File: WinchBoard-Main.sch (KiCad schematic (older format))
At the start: 26 parts, among them J1 HDMI_A, P1 CONN_01X04, P2 CONN_01X04, P3 CONN_01X04, P4 CONN_01X02, P5 CONN_01X02, P6 CONN_01X02, P7 CONN_01X03

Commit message: Checkpoint - component placement
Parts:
- added TT10, TT12: GND, _Connector:Test_Point_SMD_0.040_Top, symbol TP_Top
- added TT13: GNDA, _Connector:Test_Point_SMD_0.040_Top, symbol TP_Top
- P1, P2, P3: footprint Connectors_Molex:Molex_KK-6410-04_04x2.54mm_Straight -> _Connector:Molex_KK-6410-04_04x2.54mm_Straight
- P4, P5: footprint Connectors_Molex:Molex_KK-6410-02_02x2.54mm_Straight -> _Connector:Molex_KK-6410-02_02x2.54mm_Straight
- P6: footprint Connectors_Molex:Molex_KK-6410-02_02x2.54mm_Straight -> _Connector:0.100_1x2_small
- renumbered TT10 to TT11, TT11 to TT14
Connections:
- net GNDA: now also TT13.1 (TP)
- net GNDD: now also TT10.1 (TP), TT12.1 (TP)
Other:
- moved on the sheet: TT11, TT14
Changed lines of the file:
@@
 F 0 "P5" H 5400 4650 50  0000 C CNN
 F 1 "CONN_01X02" V 5500 4500 50  0000 C CNN
-F 2 "Connectors_Molex:Molex_KK-6410-02_02x2.54mm_Straight" H 5400 4500 50  0001 C CNN
+F 2 "_Connector:Molex_KK-6410-02_02x2.54mm_Straight" H 5400 4500 50  0001 C CNN
 F 3 "" H 5400 4500 50  0000 C CNN
 	1    5400 4500
@@
 F 0 "P3" H 4650 2900 50  0000 C CNN
 F 1 "CONN_01X04" V 4750 2650 50  0000 C CNN
-F 2 "Connectors_Molex:Molex_KK-6410-04_04x2.54mm_Straight" H 4650 2650 50  0001 C CNN
+F 2 "_Connector:Molex_KK-6410-04_04x2.54mm_Straight" H 4650 2650 50  0001 C CNN
 F 3 "" H 4650 2650 50  0000 C CNN
 	1    4650 2650
@@
 F 0 "P2" H 3650 3400 50  0000 C CNN
 F 1 "CONN_01X04" V 3750 3150 50  0000 C CNN
-F 2 "Connectors_Molex:Molex_KK-6410-04_04x2.54mm_Straight" H 3650 3150 50  0001 C CNN
+F 2 "_Connector:Molex_KK-6410-04_04x2.54mm_Straight" H 3650 3150 50  0001 C CNN
 F 3 "" H 3650 3150 50  0000 C CNN
 	1    3650 3150
@@
 L +Vanalog #PWR04
 U 1 1 5B94F6C9
-P 6750 1300
-F 0 "#PWR04" H 6750 1150 50  0001 C CNN
-F 1 "+Vanalog" H 6750 1440 50  0000 C CNN
-F 2 "" H 6750 1300 50  0000 C CNN
-F 3 "" H 6750 1300 50  0000 C CNN
-	1    6750 1300
+P 6650 1300
+F 0 "#PWR04" H 6650 1150 50  0001 C CNN
+F 1 "+Vanalog" H 6650 1440 50  0000 C CNN
+F 2 "" H 6650 1300 50  0000 C CNN
+F 3 "" H 6650 1300 50  0000 C CNN
+	1    6650 1300
 	1    0    0    -1
 $EndComp
@@
 F 0 "P1" H 2750 3900 50  0000 C CNN
 F 1 "CONN_01X04" V 2850 3650 50  0000 C CNN
-F 2 "Connectors_Molex:Molex_KK-6410-04_04x2.54mm_Straight" H 2750 3650 50  0001 C CNN
+F 2 "_Connector:Molex_KK-6410-04_04x2.54mm_Straight" H 2750 3650 50  0001 C CNN
 F 3 "" H 2750 3650 50  0000 C CNN
 	1    2750 3650
@@
 F 0 "P4" H 5150 4300 50  0000 C CNN
 F 1 "CONN_01X02" V 5250 4150 50  0000 C CNN
-F 2 "Connectors_Molex:Molex_KK-6410-02_02x2.54mm_Straight" H 5150 4150 50  0001 C CNN
+F 2 "_Connector:Molex_KK-6410-02_02x2.54mm_Straight" H 5150 4150 50  0001 C CNN
 F 3 "" H 5150 4150 50  0000 C CNN
 	1    5150 4150
@@
 	6500 2000 6800 2000
 Wire Wire Line
-	6750 1300 6750 2000
-Connection ~ 6750 2000
+	6650 1300 6650 2000
+Connection ~ 6650 2000
 Wire Wire Line
 	6500 2100 6800 2100
 Wire Wire Line
-	6750 2100 6750 2250
+	6750 1950 6750 2250
 Connection ~ 6750 2100
 Wire Wire Line
-	6800 2200 6500 2200
+	6500 2200 6800 2200
 Wire Wire Line
 	4850 2800 6100 2800
@@
 Connection ~ 6200 4400
 $Comp
-L TP_Top TT11
+L TP_Top TT14
 U 1 1 5B952A2E
-P 6950 1450
-F 0 "TT11" H 7000 1480 35  0000 C CNN
-F 1 "+Vanalog" H 6960 1580 50  0000 C CNN
-F 2 "_Connector:Test_Point_SMD_0.040_Top" H 6950 1500 50  0001 C CNN
-F 3 "" H 6950 1500 50  0000 C CNN
-	1    6950 1450
+P 6850 1450
+F 0 "TT14" H 6900 1480 35  0000 C CNN
+F 1 "+Vanalog" H 6860 1580 50  0000 C CNN
+F 2 "_Connector:Test_Point_SMD_0.040_Top" H 6850 1500 50  0001 C CNN
+F 3 "" H 6850 1500 50  0000 C CNN
+	1    6850 1450
 	1    0    0    -1
 $EndComp
@@
 $EndComp
 Wire Wire Line
-	6750 1500 6950 1500
-Wire Wire Line
-	6950 1500 6950 1450
-Connection ~ 6750 1500
+	6650 1500 6850 1500
+Wire Wire Line
+	6850 1500 6850 1450
+Connection ~ 6650 1500
 Wire Wire Line
 	6100 1500 6300 1500
@@
 F 0 "P6" H 5600 5050 50  0000 C CNN
 F 1 "CONN_01X02" V 5700 4900 50  0000 C CNN
-F 2 "Connectors_Molex:Molex_KK-6410-02_02x2.54mm_Straight" H 5600 4900 50  0001 C CNN
+F 2 "_Connector:0.100_1x2_small" H 5600 4900 50  0001 C CNN
 F 3 "" H 5600 4900 50  0000 C CNN
 	1    5600 4900
@@
 Group D Twisted Pair
 $Comp
+L TP_Top TT11
+U 1 1 5B958039
+P 6550 1900
+F 0 "TT11" H 6600 1930 35  0000 C CNN
+F 1 "Aout" H 6560 2030 50  0000 C CNN
+F 2 "_Connector:Test_Point_SMD_0.040_Top" H 6550 1950 50  0001 C CNN
+F 3 "" H 6550 1950 50  0000 C CNN
+	1    6550 1900
+	1    0    0    -1
+$EndComp
+Wire Wire Line
+	6550 1900 6550 2200
+Connection ~ 6550 2200
+$Comp
 L TP_Top TT10
-U 1 1 5B958039
-P 6550 1950
-F 0 "TT10" H 6600 1980 35  0000 C CNN
-F 1 "Aout" H 6560 2080 50  0000 C CNN
-F 2 "_Connector:Test_Point_SMD_0.040_Top" H 6550 2000 50  0001 C CNN
-F 3 "" H 6550 2000 50  0000 C CNN
-	1    6550 1950
-	1    0    0    -1
-$EndComp
-Wire Wire Line
-	6550 1950 6550 2200
-Connection ~ 6550 2200
+U 1 1 5B952974
+P 6500 4900
+F 0 "TT10" H 6550 4930 35  0000 C CNN
+F 1 "GND" H 6510 5030 50  0000 C CNN
+F 2 "_Connector:Test_Point_SMD_0.040_Top" H 6500 4950 50  0001 C CNN
+F 3 "" H 6500 4950 50  0000 C CNN
+	1    6500 4900
+	1    0    0    -1
+$EndComp
+$Comp
+L TP_Top TT12
+U 1 1 5B9529E6
+P 6750 4900
+F 0 "TT12" H 6800 4930 35  0000 C CNN
+F 1 "GND" H 6760 5030 50  0000 C CNN
+F 2 "_Connector:Test_Point_SMD_0.040_Top" H 6750 4950 50  0001 C CNN
+F 3 "" H 6750 4950 50  0000 C CNN
+	1    6750 4900
+	1    0    0    -1
+$EndComp
+Wire Wire Line
+	6500 4900 6500 4950
+Connection ~ 6500 4950
+Wire Wire Line
+	6750 4900 6750 4950
+Connection ~ 6750 4950
+$Comp
+L TP_Top TT13
+U 1 1 5B952D09
+P 6800 1900
+F 0 "TT13" H 6850 1930 35  0000 C CNN
+F 1 "GNDA" H 6810 2030 50  0000 C CNN
+F 2 "_Connector:Test_Point_SMD_0.040_Top" H 6800 1950 50  0001 C CNN
+F 3 "" H 6800 1950 50  0000 C CNN
+	1    6800 1900
+	1    0    0    -1
+$EndComp
+Wire Wire Line
+	6750 1950 6800 1950
+Wire Wire Line
+	6800 1950 6800 1900
 $EndSCHEMATC

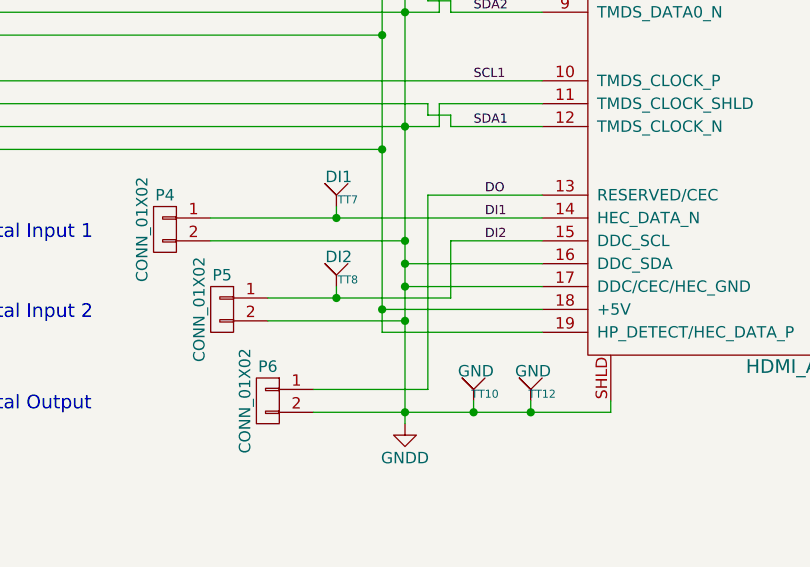
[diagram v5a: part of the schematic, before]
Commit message: Version 001 - 1.4” x 1/6” locking connectors
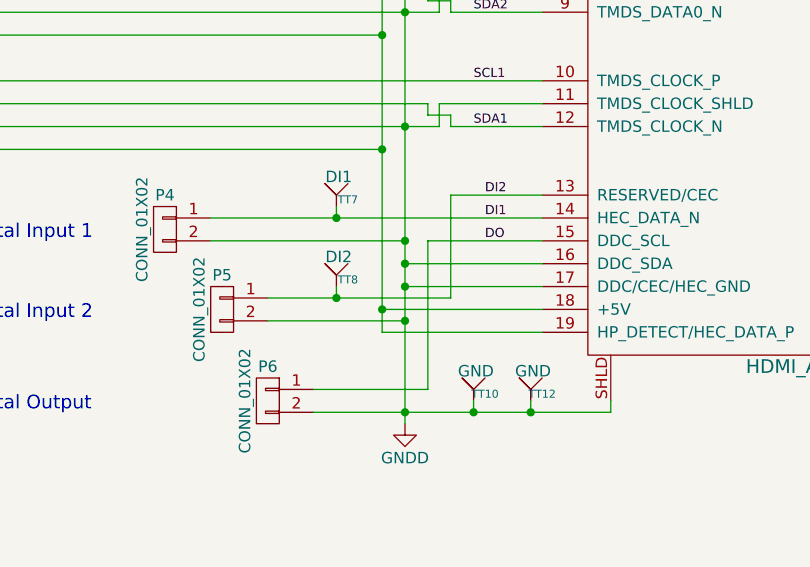
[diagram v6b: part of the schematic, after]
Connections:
- net DI2: now also J1.13 (RESERVED/CEC); no longer J1.15 (DDC_SCL)
- net DO: now also J1.15 (DDC_SCL); no longer J1.13 (RESERVED/CEC)
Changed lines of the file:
@@
-$EndComp
-$Comp
-L HDMI_A J1
-U 1 1 5B951EE4
-P 7500 3500
-F 0 "J1" H 7500 5200 60  0000 C CNN
-F 1 "HDMI_A" H 7850 2250 60  0000 C CNN
-F 2 "_Connector:FCI_10029449-11[13]RLF" H 7000 3000 60  0001 C CNN
-F 3 "" H 7000 3000 60  0000 C CNN
-	1    7500 3500
-	1    0    0    -1
 $EndComp
 $Comp
@@
 Text Label 6500 3700 0    40   ~ 0
 SDA1
-Wire Wire Line
-	6800 4300 6200 4300
 Connection ~ 6200 4300
 $Comp
@@
 Connection ~ 6200 4200
 Wire Wire Line
-	5600 4450 6400 4450
-Wire Wire Line
-	6400 4450 6400 4200
-Wire Wire Line
-	6400 4200 6800 4200
+	6400 4450 5600 4450
+Wire Wire Line
+	6400 4000 6400 4450
 Wire Wire Line
 	5600 4550 6200 4550
@@
 Text Label 6550 4100 0    40   ~ 0
 DI1
-Text Label 6550 4200 0    40   ~ 0
+Text Label 6550 4000 0    40   ~ 0
 DI2
 Wire Wire Line
@@
 	5800 4950 7100 4950
 Connection ~ 6200 4950
-Wire Wire Line
-	6300 4000 6800 4000
 $Comp
 L CONN_01X02 P6
@@
 Wire Wire Line
 	5800 4850 6300 4850
-Wire Wire Line
-	6300 4850 6300 4000
-Text Label 6550 4000 0    40   ~ 0
+Text Label 6550 4200 0    40   ~ 0
 DO
 Text Label 6600 2200 0    40   ~ 0
@@
 Wire Wire Line
 	6800 1950 6800 1900
+$Comp
+L HDMI_A J1
+U 1 1 5B951EE4
+P 7500 3500
+F 0 "J1" H 7500 5200 60  0000 C CNN
+F 1 "HDMI_A" H 7850 2250 60  0000 C CNN
+F 2 "_Connector:FCI_10029449-11[13]RLF" H 7000 3000 60  0001 C CNN
+F 3 "" H 7000 3000 60  0000 C CNN
+	1    7500 3500
+	1    0    0    -1
+$EndComp
+Wire Wire Line
+	6400 4000 6800 4000
+Wire Wire Line
+	6800 4200 6300 4200
+Wire Wire Line
+	6300 4200 6300 4850
+Wire Wire Line
+	6800 4300 6200 4300
 $EndSCHEMATC

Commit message: Double sided done for now.
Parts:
- P6: footprint _Connector:0.100_1x2_small -> _Connector:Molex_KK-6410-02_02x2.54mm_Straight
- TT1, TT10, TT11, TT12, TT13, TT14, TT2, TT3, TT4, TT5, TT6, TT7, TT8, TT9: footprint _Connector:Test_Point_SMD_0.040_Top -> _Connector:Test_Point_SMD_0.040_Bottom
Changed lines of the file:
@@
 F 0 "TT14" H 6900 1480 35  0000 C CNN
 F 1 "+Vanalog" H 6860 1580 50  0000 C CNN
-F 2 "_Connector:Test_Point_SMD_0.040_Top" H 6850 1500 50  0001 C CNN
+F 2 "_Connector:Test_Point_SMD_0.040_Bottom" H 6850 1500 50  0001 C CNN
 F 3 "" H 6850 1500 50  0000 C CNN
 	1    6850 1450
@@
 F 0 "TT9" H 6350 1480 35  0000 C CNN
 F 1 "+3.3v" H 6310 1580 50  0000 C CNN
-F 2 "_Connector:Test_Point_SMD_0.040_Top" H 6300 1500 50  0001 C CNN
+F 2 "_Connector:Test_Point_SMD_0.040_Bottom" H 6300 1500 50  0001 C CNN
 F 3 "" H 6300 1500 50  0000 C CNN
 	1    6300 1450
@@
 F 0 "TT6" H 5350 2480 35  0000 C CNN
 F 1 "SDA3" H 5310 2580 50  0000 C CNN
-F 2 "_Connector:Test_Point_SMD_0.040_Top" H 5300 2500 50  0001 C CNN
+F 2 "_Connector:Test_Point_SMD_0.040_Bottom" H 5300 2500 50  0001 C CNN
 F 3 "" H 5300 2500 50  0000 C CNN
 	1    5300 2450
@@
 F 0 "TT5" H 5050 2480 35  0000 C CNN
 F 1 "SCL3" H 5010 2580 50  0000 C CNN
-F 2 "_Connector:Test_Point_SMD_0.040_Top" H 5000 2500 50  0001 C CNN
+F 2 "_Connector:Test_Point_SMD_0.040_Bottom" H 5000 2500 50  0001 C CNN
 F 3 "" H 5000 2500 50  0000 C CNN
 	1    5000 2450
@@
 F 0 "TT3" H 4000 2980 35  0000 C CNN
 F 1 "SCL2" H 3960 3080 50  0000 C CNN
-F 2 "_Connector:Test_Point_SMD_0.040_Top" H 3950 3000 50  0001 C CNN
+F 2 "_Connector:Test_Point_SMD_0.040_Bottom" H 3950 3000 50  0001 C CNN
 F 3 "" H 3950 3000 50  0000 C CNN
 	1    3950 2950
@@
 F 0 "TT4" H 4300 2980 35  0000 C CNN
 F 1 "SDA2" H 4260 3080 50  0000 C CNN
-F 2 "_Connector:Test_Point_SMD_0.040_Top" H 4250 3000 50  0001 C CNN
+F 2 "_Connector:Test_Point_SMD_0.040_Bottom" H 4250 3000 50  0001 C CNN
 F 3 "" H 4250 3000 50  0000 C CNN
 	1    4250 2950
@@
 F 0 "TT1" H 3050 3480 35  0000 C CNN
 F 1 "SCL1" H 3010 3580 50  0000 C CNN
-F 2 "_Connector:Test_Point_SMD_0.040_Top" H 3000 3500 50  0001 C CNN
+F 2 "_Connector:Test_Point_SMD_0.040_Bottom" H 3000 3500 50  0001 C CNN
 F 3 "" H 3000 3500 50  0000 C CNN
 	1    3000 3450
@@
 F 0 "TT2" H 3350 3480 35  0000 C CNN
 F 1 "SDA1" H 3310 3580 50  0000 C CNN
-F 2 "_Connector:Test_Point_SMD_0.040_Top" H 3300 3500 50  0001 C CNN
+F 2 "_Connector:Test_Point_SMD_0.040_Bottom" H 3300 3500 50  0001 C CNN
 F 3 "" H 3300 3500 50  0000 C CNN
 	1    3300 3450
@@
 F 0 "TT7" H 5950 4080 35  0000 C CNN
 F 1 "DI1" H 5910 4180 50  0000 C CNN
-F 2 "_Connector:Test_Point_SMD_0.040_Top" H 5900 4100 50  0001 C CNN
+F 2 "_Connector:Test_Point_SMD_0.040_Bottom" H 5900 4100 50  0001 C CNN
 F 3 "" H 5900 4100 50  0000 C CNN
 	1    5900 4050
@@
 F 0 "TT8" H 5950 4430 35  0000 C CNN
 F 1 "DI2" H 5910 4530 50  0000 C CNN
-F 2 "_Connector:Test_Point_SMD_0.040_Top" H 5900 4450 50  0001 C CNN
+F 2 "_Connector:Test_Point_SMD_0.040_Bottom" H 5900 4450 50  0001 C CNN
 F 3 "" H 5900 4450 50  0000 C CNN
 	1    5900 4400
@@
 F 0 "P6" H 5600 5050 50  0000 C CNN
 F 1 "CONN_01X02" V 5700 4900 50  0000 C CNN
-F 2 "_Connector:0.100_1x2_small" H 5600 4900 50  0001 C CNN
+F 2 "_Connector:Molex_KK-6410-02_02x2.54mm_Straight" H 5600 4900 50  0001 C CNN
 F 3 "" H 5600 4900 50  0000 C CNN
 	1    5600 4900
@@
 F 0 "TT11" H 6600 1930 35  0000 C CNN
 F 1 "Aout" H 6560 2030 50  0000 C CNN
-F 2 "_Connector:Test_Point_SMD_0.040_Top" H 6550 1950 50  0001 C CNN
+F 2 "_Connector:Test_Point_SMD_0.040_Bottom" H 6550 1950 50  0001 C CNN
 F 3 "" H 6550 1950 50  0000 C CNN
 	1    6550 1900
@@
 F 0 "TT10" H 6550 4930 35  0000 C CNN
 F 1 "GND" H 6510 5030 50  0000 C CNN
-F 2 "_Connector:Test_Point_SMD_0.040_Top" H 6500 4950 50  0001 C CNN
+F 2 "_Connector:Test_Point_SMD_0.040_Bottom" H 6500 4950 50  0001 C CNN
 F 3 "" H 6500 4950 50  0000 C CNN
 	1    6500 4900
@@
 F 0 "TT12" H 6800 4930 35  0000 C CNN
 F 1 "GND" H 6760 5030 50  0000 C CNN
-F 2 "_Connector:Test_Point_SMD_0.040_Top" H 6750 4950 50  0001 C CNN
+F 2 "_Connector:Test_Point_SMD_0.040_Bottom" H 6750 4950 50  0001 C CNN
 F 3 "" H 6750 4950 50  0000 C CNN
 	1    6750 4900
@@
 F 0 "TT13" H 6850 1930 35  0000 C CNN
 F 1 "GNDA" H 6810 2030 50  0000 C CNN
-F 2 "_Connector:Test_Point_SMD_0.040_Top" H 6800 1950 50  0001 C CNN
+F 2 "_Connector:Test_Point_SMD_0.040_Bottom" H 6800 1950 50  0001 C CNN
 F 3 "" H 6800 1950 50  0000 C CNN
 	1    6800 1900

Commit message: Semi-final commit before fab
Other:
- note added: "Note: There are no I2C termination resistors on this board.\nIt is assumed that these are on the other end of the line."
- note removed: "Note: There are no I2C termination resistors on this board.\nIt is assumd that these are on the other end of the line."
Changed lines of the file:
@@
 	5300 2450 5300 2600
 Connection ~ 5300 2600
-Text Notes 1800 4150 0    40   ~ 0
-Note: There are no I2C termination resistors on this board.\nIt is assumd that these are on the other end of the line.
+Text Notes 1850 4150 0    40   ~ 0
+Note: There are no I2C termination resistors on this board.\nIt is assumed that these are on the other end of the line.
 $Comp
 L TP_Top TT3
